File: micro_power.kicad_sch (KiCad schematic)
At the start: 28 parts, among them J7 4840.2201, J8 20021111-00010T4LF, J9 75869-105LF, Q1 BSS308PE, SW1 1825910-6, SW2 A11AH, U10 LM1086CS-5.0, U11 STM32G051K8T6, U9 LM1086CS-3.3, Y2 ABLS2-8.000MHZ-D4Y-T

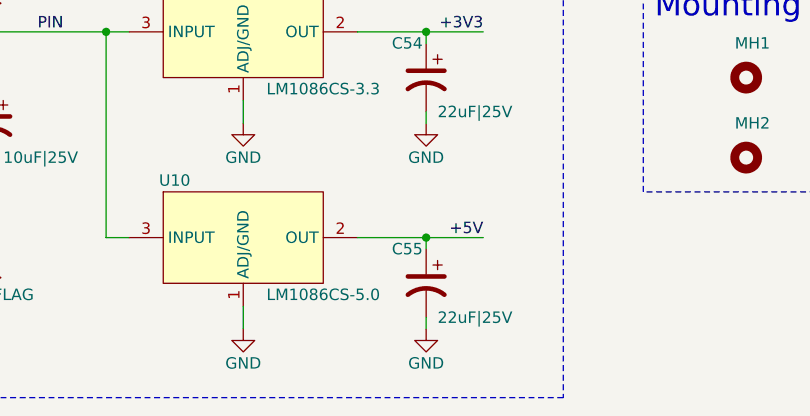
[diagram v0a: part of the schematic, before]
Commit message: updates from library, performed ERC/DRC, update Kicad 8.0.8
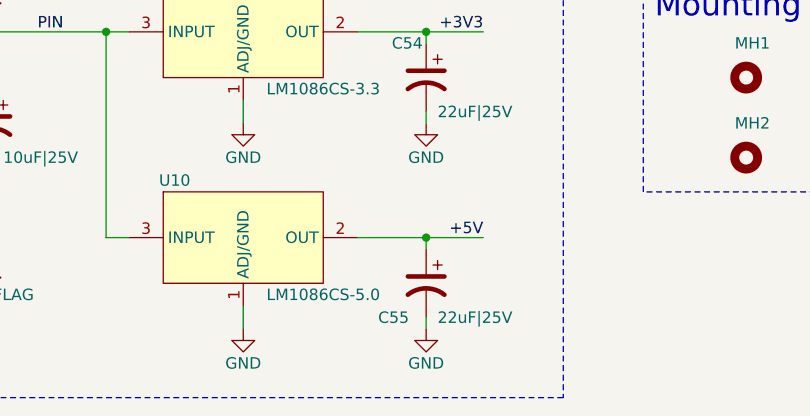
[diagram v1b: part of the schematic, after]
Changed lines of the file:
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@@
 	(label "EXP_8"
 		(at 196.85 93.98 180)
-		(fields_autoplaced yes)
 		(effects
 			(font
@@
 	(label "EXP_4"
 		(at 196.85 83.82 180)
-		(fields_autoplaced yes)
 		(effects
 			(font
@@
 	(label "EXP_5"
 		(at 196.85 86.36 180)
-		(fields_autoplaced yes)
 		(effects
 			(font
@@
 	(label "EXP_1"
 		(at 196.85 68.58 180)
-		(fields_autoplaced yes)
 		(effects
 			(font
@@
 	(label "+5V"
 		(at 158.75 163.83 180)
-		(fields_autoplaced yes)
 		(effects
 			(font
@@
 	(label "MEM_CLR"
 		(at 196.85 106.68 180)
-		(fields_autoplaced yes)
 		(effects
 			(font
@@
 	(label "D_50HZ"
 		(at 196.85 63.5 180)
-		(fields_autoplaced yes)
 		(effects
 			(font
@@
 	(label "D_SIGNAL"
 		(at 196.85 58.42 180)
-		(fields_autoplaced yes)
 		(effects
 			(font
@@
 	(label "EXP_9"
 		(at 196.85 96.52 180)
-		(fields_autoplaced yes)
 		(effects
 			(font
@@
 	(label "RENC_B"
 		(at 196.85 78.74 180)
-		(fields_autoplaced yes)
 		(effects
 			(font
@@
 	(label "D_60HZ"
 		(at 196.85 66.04 180)
-		(fields_autoplaced yes)
 		(effects
 			(font
@@
 	(label "D_READY"
 		(at 196.85 55.88 180)
-		(fields_autoplaced yes)
 		(effects
 			(font
@@
 	(label "RENC_SW"
 		(at 196.85 81.28 180)
-		(fields_autoplaced yes)
 		(effects
 			(font
@@
 	(label "VENC_RST"
 		(at 196.85 101.6 180)
-		(fields_autoplaced yes)
 		(effects
 			(font
@@
 	(label "EXP_2"
 		(at 196.85 71.12 180)
-		(fields_autoplaced yes)
 		(effects
 			(font
@@
 	(label "PIN"
 		(at 109.22 140.97 0)
-		(fields_autoplaced yes)
 		(effects
 			(font
@@
 	(label "SCL2"
 		(at 209.55 50.8 0)
-		(fields_autoplaced yes)
 		(effects
 			(font
@@
 	(label "EXP_3"
 		(at 196.85 73.66 180)
-		(fields_autoplaced yes)
 		(effects
 			(font
@@
 	(label "EXP_7"
 		(at 196.85 91.44 180)
-		(fields_autoplaced yes)
 		(effects
 			(font
@@
 	(label "MEM_MODE"
 		(at 196.85 104.14 180)
-		(fields_autoplaced yes)
 		(effects
 			(font
@@
 	(label "SDA2"
 		(at 209.55 53.34 0)
-		(fields_autoplaced yes)
 		(effects
 			(font
@@
 	(label "VDEC_RST"
 		(at 196.85 99.06 180)
-		(fields_autoplaced yes)
 		(effects
 			(font
@@
 	(label "EXP_6"
 		(at 196.85 88.9 180)
-		(fields_autoplaced yes)
 		(effects
 			(font
@@
 	(label "D_INTERLACED"
 		(at 196.85 60.96 180)
-		(fields_autoplaced yes)
 		(effects
 			(font
@@
 	(label "+3V3"
 		(at 158.75 140.97 180)
-		(fields_autoplaced yes)
 		(effects
 			(font
@@
 	(label "RENC_A"
 		(at 196.85 76.2 180)
-		(fields_autoplaced yes)
 		(effects
 			(font
@@
 	(label "SDA2"
 		(at 72.39 93.98 0)
-		(fields_autoplaced yes)
 		(effects
 			(font
@@
 	(label "SCL2"
 		(at 72.39 91.44 0)
-		(fields_autoplaced yes)
 		(effects
 			(font
@@
 		(shape output)
 		(at 201.93 106.68 0)
-		(fields_autoplaced yes)
 		(effects
 			(font
@@
 		(shape output)
 		(at 77.47 104.14 180)
-		(fields_autoplaced yes)
 		(effects
 			(font
@@
 		(shape output)
 		(at 208.28 48.26 180)
-		(fields_autoplaced yes)
 		(effects
 			(font
@@
 		(shape bidirectional)
 		(at 77.47 106.68 180)
-		(fields_autoplaced yes)
 		(effects
 			(font
@@
 		(shape output)
 		(at 201.93 104.14 0)
-		(fields_autoplaced yes)
 		(effects
 			(font
@@
 		(shape output)
 		(at 201.93 101.6 0)
-		(fields_autoplaced yes)
 		(effects
 			(font
@@
 		(shape output)
 		(at 201.93 99.06 0)
-		(fields_autoplaced yes)
 		(effects
 			(font
@@
 			)
 		)
+		(property "Sim.Enable" "0"
+			(at 81.28 87.376 0)
+			(effects
+				(font
+					(size 1.27 1.27)
+				)
+				(hide yes)
+			)
+		)
 		(pin "1"
 		)
@@
 		(dnp no)
 		(property "Reference" "C55"
-			(at 148.59 165.1 90)
+			(at 147.066 172.72 90)
 			(effects
 				(font
@@
 			)
 		)
-		(property "Description" ""
+		(property "Description" "Tantalum Capacitors - Solid SMD 22uF 25volts 10% D case Molded"
 			(at 152.4 168.91 0)
 			(effects
@@
 			)
 		)
+		(property "Sim.Enable" "0"
+			(at 137.16 168.91 0)
+			(effects
+				(font
+					(size 1.27 1.27)
+				)
+				(hide yes)
+			)
+		)
 		(pin "1"
 		)
@@
 			)
 		)
+		(property "Sim.Enable" "0"
+			(at 68.58 59.436 0)
+			(effects
+				(font
+					(size 1.27 1.27)
+				)
+				(hide yes)
+			)
+		)
 		(pin "1"
 		)
@@
 			)
 		)
+		(property "Sim.Enable" "0"
+			(at 214.63 41.656 0)
+			(effects
+				(font
+					(size 1.27 1.27)
+				)
+				(hide yes)
+			)
+		)
 		(pin "1"
 		)
@@
 			)
 		)
-		(property "Description" ""
+		(property "Description" "Tantalum Capacitors - Solid SMD 22uF 25volts 10% D case Molded"
 			(at 152.4 146.05 0)
 			(effects
@@
 			)
 		)
+		(property "Sim.Enable" "0"
+			(at 137.16 146.05 0)
+			(effects
+				(font
+					(size 1.27 1.27)
+				)
+				(hide yes)
+			)
+		)
 		(pin "1"
 		)
@@
 			)
 		)
+		(property "Sim.Enable" "0"
+			(at 158.75 41.656 0)
+			(effects
+				(font
+					(size 1.27 1.27)
+				)
+				(hide yes)
+			)
+		)
 		(pin "1"
 		)
@@
 			(effects
 				(font
+					(size 1.27 1.27)
+				)
+				(hide yes)
+			)
+		)
+		(property "Sim.Enable" "0"
+			(at 85.09 59.436 0)
+			(effects
+				(font
